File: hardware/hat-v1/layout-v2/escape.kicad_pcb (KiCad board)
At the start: 4 copper layers, 65 x 56.5 mm, 86 parts, among them J1 BATT pads, J2 Pi 40-pin (female, 11 mm stac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, J3 mPCIe 5.2H, J4 U.FL, Q1 CSD19537Q3, Q2 BSS138, Q3 CSD17578Q3A, Q6 BSS138, U1 TPS26631RGER, U14 MAX-M10S-00B, U2 INA226AIDGSR, U3 LMR33640DDDAR, U4 LM74700QDBVRQ1, U7 TPS62933FDRLR, U8 INA226AIDGSR

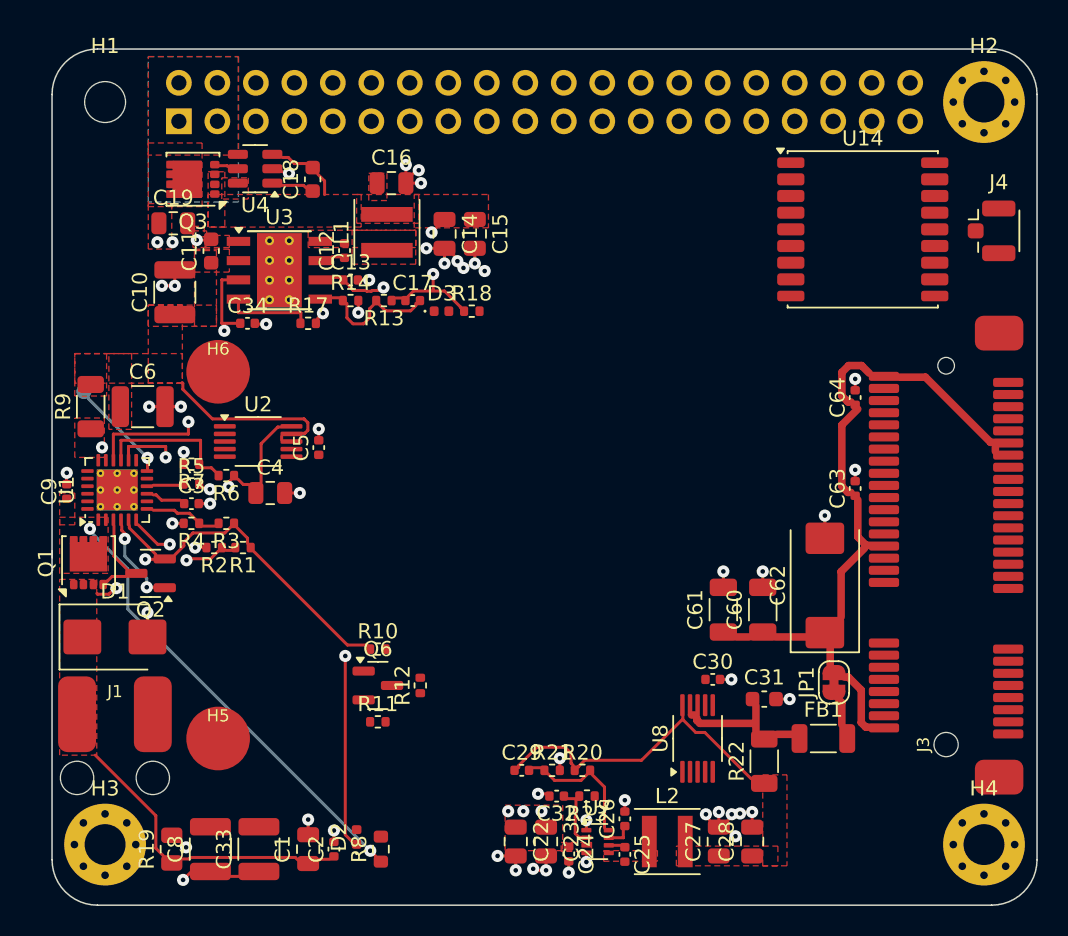
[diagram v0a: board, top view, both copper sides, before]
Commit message: HAT v1 layout v2: real Würth standoff in the escape proof; H6 corner fix; Freerouting G2 preview
- src_board.py: copy of the main board with footprints swapped to match design.py (H5/H6 ->
  Wurth WA-SMSI M2); export_fp.py / escape.py read SRC_BOARD and print the board they load.
- H5/H6 standoffs: Würth 9774030243R footprint (pad D5.3 + NPTH D3.0), design.py / gen_fp.py.
- G0 conflicts from the 5.8 courtyard fixed by a min-displacement search (C6/R9, U2/R6, C34);
  review fixes: EN_5V hand track follows C34, J1 not moved (J1 x H5 courtyard_exempt, sketch.py
  supports it), no-via ring r3.05 and NPTH keep-out r1.8 around H5/H6 in escape.py.
- Full escape: power 31/31 routed, VSYS necks 1.90 / 1.19 mm, 0 vias within r3.05 of H5/H6,
  remaining signals 45/65 (escape-full.log).
- frpreview.py + frprev/run2.sh: Freerouting on the escape board with only the planned power
  copper kept. Two runs: 102 / 95 unconnected (DRC), concentrated outside the power zones
  (card underside Z5/Z6, J3 side, GNSS, top strip). G1 on hold (PLAN §13).
- PLAN §12 (+3 mm left, power re-place) kept as a reviewed backup plan; HANDOFF §9.

Co-Authored-By: Claude Opus 5.5 <noreply@anthropic.com>
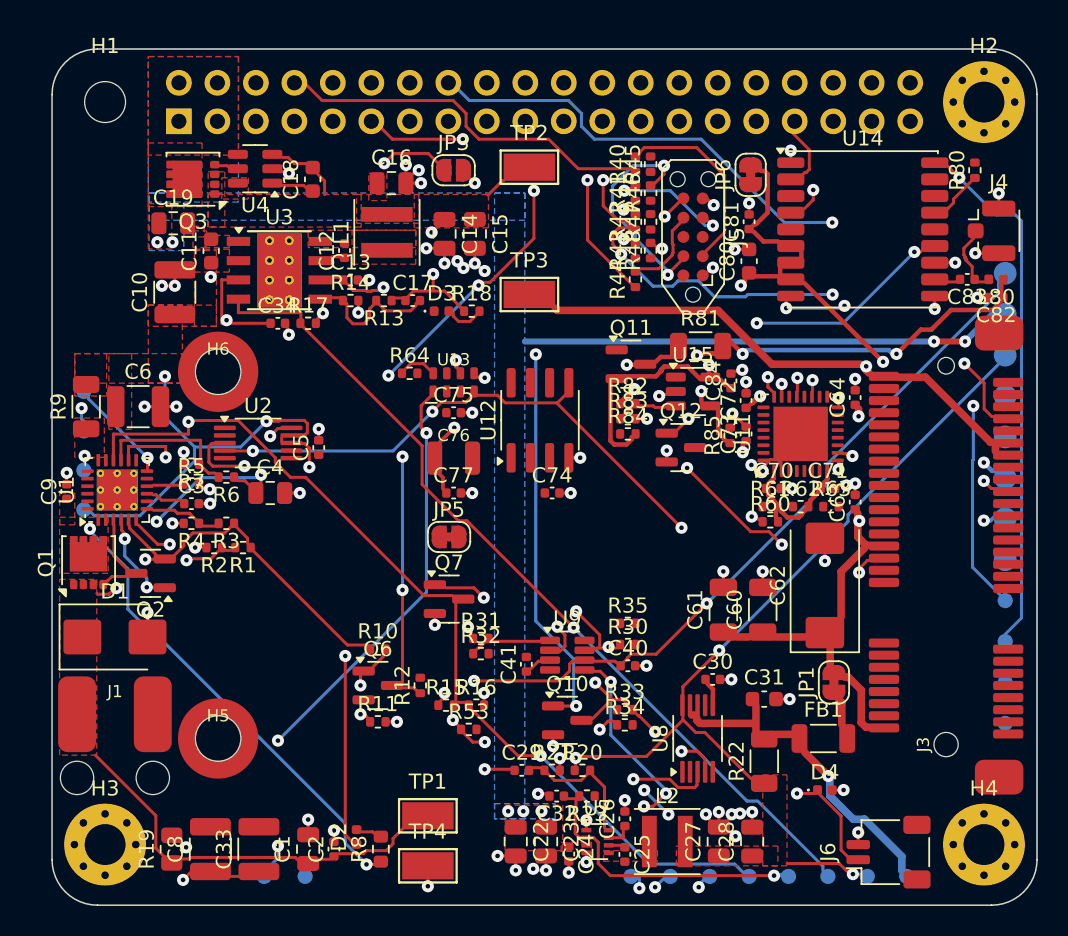
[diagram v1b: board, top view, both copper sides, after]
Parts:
- added C40: 100n 50V X7R, C_0402_1005Metric, F.Cu at (138.0, 140.7)
- added C41: 1u 10V, C_0402_1005Metric, F.Cu at (131.3, 140.6)
- added C70: 100n 16V, C_0402_1005Metric, F.Cu at (147.6, 129.0)
- added C71: 100n 16V, C_0402_1005Metric, F.Cu at (151.2, 129.0)
- added C72: 100n 16V, C_0402_1005Metric, F.Cu at (145.8, 123.2)
- added C73: 1u 10V, C_0402_1005Metric, F.Cu at (145.8, 125.4)
- added C74: 100n 16V, C_0402_1005Metric, F.Cu at (133.0, 129.3)
- added C75: 100n 16V, C_0402_1005Metric, F.Cu at (126.5, 124.0)
- added C76: CPH3225A 11mF, Seiko_CPH3225A, F.Cu at (126.5, 127.0)
- added C77: 100n 16V, C_0402_1005Metric, F.Cu at (126.5, 129.3)
- added C80: 10u 10V, C_0603_1608Metric, F.Cu at (146.0, 114.0)
- added C81: 100n 16V, C_0402_1005Metric, F.Cu at (146.0, 111.4)
- added C82: 10n 16V X7R, C_0402_1005Metric, F.Cu at (162.3, 116.4)
- added C83: 47p C0G, C_0402_1005Metric, F.Cu at (160.4, 115.2)
- added C84: 100n 16V, C_0402_1005Metric, F.Cu at (144.8, 121.9)
- added D4: TPD1E10B06, D_0402_1005Metric, F.Cu at (151.0, 148.9)
- added J5: Tag-Connect TC2050, Tag-Connect_TC2050-IDC-NL_2x05_P1.27mm_Vertical, F.Cu at (142.3, 112.4)
- added J6: PANEL BTN, JST_SH_SM02B-SRSS-TB_1x02-1MP_P1.00mm_Horizontal, F.Cu at (155.2, 153.0)
- added JP3: AUTO-ON (open), SolderJumper-2_P1.3mm_Open_RoundedPad1.0x1.5mm, F.Cu at (126.5, 108.0)
- added JP5: SEC (closed), SolderJumper-2_P1.3mm_Bridged_RoundedPad1.0x1.5mm, F.Cu at (126.2, 132.2)
- added JP6: GNSS (closed), SolderJumper-2_P1.3mm_Bridged_RoundedPad1.0x1.5mm, F.Cu at (146.1, 108.3)
- added L80: 27nH, L_0402_1005Metric, F.Cu at (162.3, 115.2)
- added Q10: BSS138, SOT-23, F.Cu at (134.0, 144.3)
- added Q11: Si2301CDS, SOT-23, F.Cu at (138.2, 120.8)
- added Q12: BSS138, SOT-23, F.Cu at (141.5, 126.3)
- added Q7: BSS138, SOT-23, F.Cu at (126.2, 136.3)
- added R15: 102k 1%, R_0402_1005Metric, F.Cu at (126.0, 143.3)
- added R16: 24.3k 1%, R_0402_1005Metric, F.Cu at (128.0, 143.3)
- added R30: 1M, R_0402_1005Metric, F.Cu at (138.0, 139.3)
- added R31: 787k 1%, R_0402_1005Metric, F.Cu at (128.3, 138.9)
- added R32: 100k 1%, R_0402_1005Metric, F.Cu at (128.3, 139.9)
- added R33: 10k, R_0402_1005Metric, F.Cu at (137.8, 143.6)
- added R34: 100k, R_0402_1005Metric, F.Cu at (137.8, 144.6)
- added R35: 10k, R_0402_1005Metric, F.Cu at (138.0, 137.9)
- added R40: 0R, R_0402_1005Metric, F.Cu at (138.5, 107.6)
- added R41: 0R, R_0402_1005Metric, F.Cu at (138.5, 109.5)
- added R42: 0R, R_0402_1005Metric, F.Cu at (138.5, 111.4)
- added R43: 0R, R_0402_1005Metric, F.Cu at (138.5, 113.3)
- added R44: 0R, R_0402_1005Metric, F.Cu at (138.5, 115.2)
- added R45: 0R, R_0402_1005Metric, F.Cu at (139.5, 107.6)
- added R46: 0R, R_0402_1005Metric, F.Cu at (139.5, 109.5)
- added R47: 0R, R_0402_1005Metric, F.Cu at (139.5, 111.4)
- added R48: 1k, R_0402_1005Metric, F.Cu at (139.5, 113.3)
- added R53: 10k, R_0402_1005Metric, F.Cu at (127.5, 144.9)
- added R60: 10k, R_0402_1005Metric, F.Cu at (147.4, 131.2)
- added R61: 10k, R_0402_1005Metric, F.Cu at (147.4, 130.2)
- added R62: 10k, R_0402_1005Metric, F.Cu at (149.4, 130.2)
- added R63: 10k, R_0402_1005Metric, F.Cu at (151.4, 130.2)
- added R64: 100k, R_0402_1005Metric, F.Cu at (123.6, 121.4)
- added R80: DNP 0R, R_0402_1005Metric, F.Cu at (160.9, 108.0)
- added R81: 10R, R_1206_3216Metric, F.Cu at (142.8, 119.6)
- added R82: 560R, R_0402_1005Metric, F.Cu at (138.0, 123.4)
- added R83: 100k, R_0402_1005Metric, F.Cu at (138.0, 124.4)
- added R84: 100k, R_0402_1005Metric, F.Cu at (138.0, 125.4)
- added R85: 1k, R_0402_1005Metric, F.Cu at (144.8, 125.5)
- added TP1: VBAT 6-17V, TestPoint_Keystone_5015_Micro-Minature, F.Cu at (124.8, 150.6)
- added TP10: 3V3_GNSS 3.2-3.4, TestPoint_Pad_D1.5mm, B.Cu at (162.9, 128.3)
- added TP11: VRTC 0-3.3, TestPoint_Pad_D1.5mm, B.Cu at (162.9, 131.0)
- added TP12: GND, TestPoint_Pad_D1.5mm, B.Cu at (162.9, 133.7)
- added TP13: GNSS_RST_N, TestPoint_Pad_D1.0mm, B.Cu at (162.9, 136.4)
- added TP14: GNSS_SAFEBOOT_N, TestPoint_Pad_D1.0mm, B.Cu at (162.9, 139.1)
- added TP15: GNSS_ANT_DET, TestPoint_Pad_D1.0mm, B.Cu at (162.9, 141.8)
- added TP16: GNSS_ANT_SHORT_N, TestPoint_Pad_D1.0mm, B.Cu at (162.9, 144.5)
- added TP17: PWR_BTN_N, TestPoint_Pad_D1.0mm, B.Cu at (138.2, 154.6)
- added TP18: LTC_KILL_N, TestPoint_Pad_D1.0mm, B.Cu at (140.8, 154.6)
- added TP19: LTC_ENB, TestPoint_Pad_D1.0mm, B.Cu at (143.4, 154.6)
- added TP2: 5V 5.10-5.25, TestPoint_Keystone_5015_Micro-Minature, F.Cu at (131.5, 107.8)
- added TP20: EN_5V, TestPoint_Pad_D1.0mm, B.Cu at (146.0, 154.6)
- added TP21: EN_3V3, TestPoint_Pad_D1.0mm, B.Cu at (148.6, 154.6)
- added TP22: PG_5V, TestPoint_Pad_D1.0mm, B.Cu at (151.2, 154.6)
- added TP23: EF_FLT_N, TestPoint_Pad_D1.0mm, B.Cu at (102.1, 125.2)
- added TP25: RTC_CLKOUT, TestPoint_Pad_D1.0mm, B.Cu at (114.0, 154.6)
- added TP26: RTC_INT_N, TestPoint_Pad_D1.0mm, B.Cu at (116.7, 154.6)
- added TP27: K1+ (R9), TestPoint_Pad_D1.0mm, B.Cu at (102.1, 127.8)
- added TP28: K1- (R9), TestPoint_Pad_D1.0mm, B.Cu at (102.1, 130.4)
- added TP29: K2+ (R22), TestPoint_Pad_D1.0mm, B.Cu at (153.8, 154.6)
- added TP3: 3V3 HaLow 3.2-3.4, TestPoint_Keystone_5015_Micro-Minature, F.Cu at (131.5, 116.2)
- added TP30: K2- (R22), TestPoint_Pad_D1.0mm, B.Cu at (156.4, 154.6)
- added TP4: GND, TestPoint_Keystone_5015_Micro-Minature, F.Cu at (124.8, 153.9)
- added TP5: VSYS 6-17V, TestPoint_Pad_D1.5mm, B.Cu at (162.9, 114.8)
- added TP6: 5V_PI 5.0-5.2, TestPoint_Pad_D1.5mm, B.Cu at (162.9, 117.5)
- added TP7: 3V3_BUCK 3.25-3.40, TestPoint_Pad_D1.5mm, B.Cu at (162.9, 120.2)
- added TP8: 3V3_PI 3.2-3.4, TestPoint_Pad_D1.5mm, B.Cu at (162.9, 122.9)
- added TP9: 3V3_SEC 3.2-3.4, TestPoint_Pad_D1.5mm, B.Cu at (162.9, 125.6)
- added U11: SLB9672XU2.0, QFN-32-1EP_5x5mm_P0.5mm_EP3.6x3.6mm, F.Cu at (149.4, 125.4)
- added U12: ATECC608C-TFLXTLS, SOIC-8_3.9x4.9mm_P1.27mm, F.Cu at (132.2, 124.5)
- added U13: RV-3028-C7, MicroCrystal_RV-3028-C7, F.Cu at (126.5, 122.0)
- added U15: OPA333AIDBVR, SOT-23-5, F.Cu at (142.3, 122.6)
- added U9: LTC2955ITS8-2#TRPBF, TSOT-23-8, F.Cu at (134.0, 140.0)
- H5, H6: footprint SMT_Standoff_M2_TBD -> batman:Wurth_WA-SMSI_M2_OD4.35
- moved C34 2.00 mm to (114.9, 118.1)
- moved C63 0.90 mm to (153.0, 129.9)
- moved C6 0.30 mm to (105.7, 123.6)
- moved R9 0.30 mm to (102.2, 123.6)
- moved R6 0.10 mm to (111.5, 128.2)
- moved U2 0.10 mm to (113.6, 126.0)
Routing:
- net VSYS: track 10.9 -> 111.1 mm, vias 0 -> 8
- net INA_ALERT_N: track 0.00 -> 80.4 mm, vias 0 -> 7
- net I2C1_SDA: track 0.00 -> 74.1 mm, vias 0 -> 4
- net EN_5V: track 18.8 -> 72.7 mm, vias 2 -> 3
- net HALOW_WAKE: track 0.00 -> 52.6 mm, vias 0 -> 2
- net PG_5V: track 5.32 -> 56.1 mm, vias 0 -> 1
- net HALOW_RESET_N: track 0.00 -> 48.8 mm, vias 0 -> 4
- net KILL_REQ: track 0.00 -> 46.9 mm, vias 0 -> 3
- net VRTC: track 0.00 -> 45.9 mm, vias 0 -> 3
- net BAT_PRESENT_N: track 0.00 -> 45.5 mm, vias 0 -> 2
- net 3V3_GNSS: track 0.00 -> 45.0 mm, vias 0 -> 4
- net SPI0_SCLK: track 0.00 -> 40.7 mm, vias 0 -> 4
- net 3V3_BUCK: track 19.6 -> 58.1 mm, vias 0 -> 4
- net RTC_CLKOUT: track 0.00 -> 36.0 mm, vias 0 -> 3
- net GNSS_SAFEBOOT_N: track 0.00 -> 34.1 mm, vias 0 -> 1
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- removed copper zone on In2.Cu, net 5V_PI
